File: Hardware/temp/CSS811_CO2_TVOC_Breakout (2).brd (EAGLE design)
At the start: 17.8 x 17.8 mm, 20 parts, among them U2 CCS811

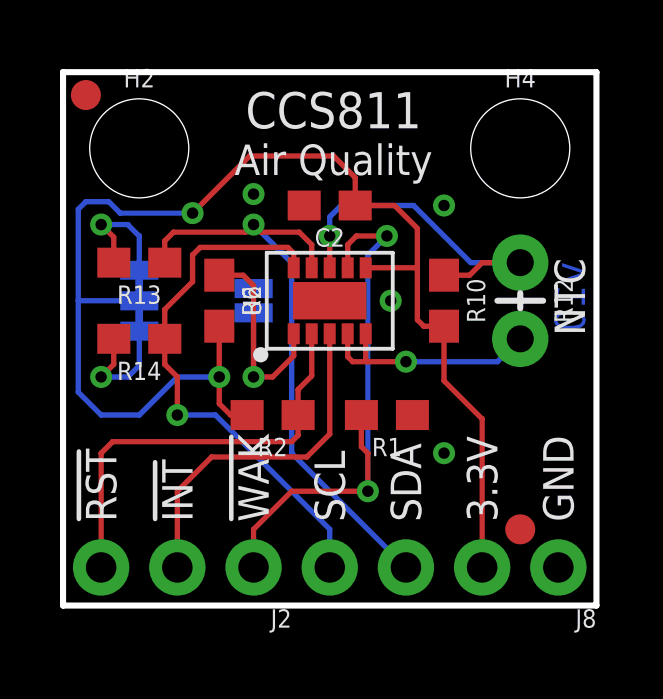
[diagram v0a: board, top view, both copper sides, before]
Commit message: Added temp library of new parts, added proper gitignore/gitattributes, switched sparkfun logo in for sparkx logo, cleaned up schematic, changed version number to v10
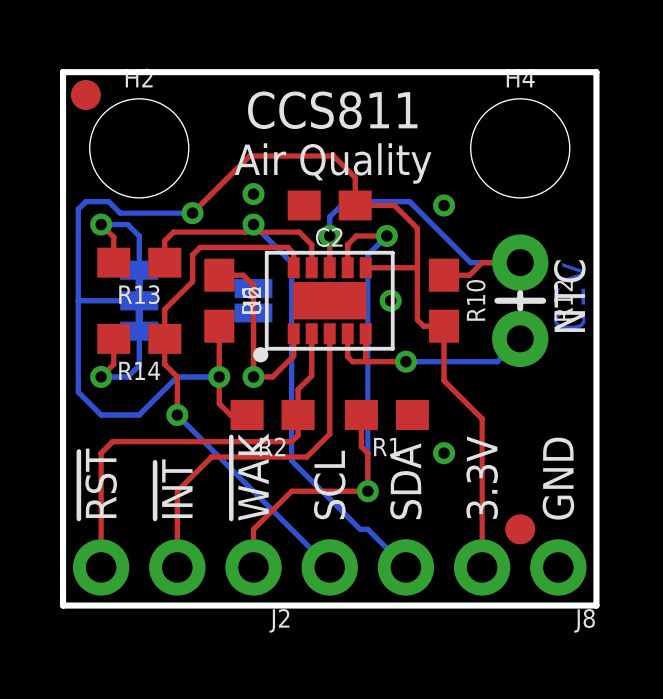
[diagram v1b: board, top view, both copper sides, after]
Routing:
- net SCL: track 17.9 -> 17.1 mm
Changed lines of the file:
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@@
 <layer number="21" name="tPlace" color="16" fill="1" visible="no" active="yes"/>
 <layer number="22" name="bPlace" color="14" fill="1" visible="yes" active="yes"/>
-<layer number="23" name="tOrigins" color="15" fill="1" visible="no" active="yes"/>
+<layer number="23" name="tOrigins" color="15" fill="1" visible="yes" active="yes"/>
 <layer number="24" name="bOrigins" color="15" fill="1" visible="yes" active="yes"/>
 <layer number="25" name="tNames" color="7" fill="1" visible="no" active="yes"/>
@@
 <wire x1="3.81" y1="7.62" x2="3.81" y2="6.35" width="0.1778" layer="1"/>
 <via x="3.81" y="6.35" extent="1-16" drill="0.381"/>
-<wire x1="3.81" y1="6.35" x2="5.08" y2="6.35" width="0.1778" layer="16"/>
-<wire x1="5.08" y1="6.35" x2="8.89" y2="2.54" width="0.1778" layer="16"/>
-<wire x1="8.89" y1="2.54" x2="8.89" y2="1.27" width="0.1778" layer="16"/>
+<wire x1="3.81" y1="6.35" x2="8.89" y2="1.27" width="0.1778" layer="16"/>
 <contactref element="U2" pad="10"/>
 <wire x1="7.69" y1="11.26" x2="7.69" y2="11.741" width="0.1778" layer="1"/>
@@
 <wire x1="3.683" y1="12.446" x2="3.39" y2="12.153" width="0.1778" layer="1"/>
 <wire x1="3.39" y1="11.43" x2="3.39" y2="12.153" width="0.1778" layer="1"/>
-<wire x1="11.43" y1="1.27" x2="7.62" y2="5.08" width="0.1778" layer="16"/>
+<wire x1="11.43" y1="1.27" x2="10.16" y2="2.54" width="0.1778" layer="16"/>
+<wire x1="10.16" y1="2.54" x2="9.906" y2="2.54" width="0.1778" layer="16"/>
+<wire x1="9.906" y1="2.54" x2="7.62" y2="4.826" width="0.1778" layer="16"/>
 <via x="6.35" y="12.7" extent="1-16" drill="0.381"/>
 <contactref element="U2" pad="9"/>
@@
 <wire x1="3.683" y1="12.446" x2="6.096" y2="12.446" width="0.1778" layer="1"/>
 <wire x1="6.096" y1="12.446" x2="6.35" y2="12.7" width="0.1778" layer="1"/>
-<wire x1="7.62" y1="5.08" x2="7.62" y2="11.43" width="0.1778" layer="16"/>
+<wire x1="7.62" y1="4.826" x2="7.62" y2="11.43" width="0.1778" layer="16"/>
 <wire x1="7.62" y1="11.43" x2="6.35" y2="12.7" width="0.1778" layer="16"/>
 </signal>
@@
 <contactref element="U2" pad="8"/>
 <wire x1="8.89" y1="11.26" x2="8.89" y2="12.319" width="0.1778" layer="1"/>
-<wire x1="9.271" y1="13.335" x2="8.89" y2="12.954" width="0.1778" layer="16"/>
+<wire x1="9.398" y1="13.462" x2="8.89" y2="12.954" width="0.1778" layer="16"/>
 <wire x1="8.89" y1="12.954" x2="8.89" y2="12.319" width="0.1778" layer="16"/>
 <wire x1="15.24" y1="11.43" x2="13.589" y2="11.43" width="0.1778" layer="16"/>
-<wire x1="13.589" y1="11.43" x2="11.684" y2="13.335" width="0.1778" layer="16"/>
-<wire x1="11.684" y1="13.335" x2="9.271" y2="13.335" width="0.1778" layer="16"/>
+<wire x1="13.589" y1="11.43" x2="11.557" y2="13.462" width="0.1778" layer="16"/>
+<wire x1="11.557" y1="13.462" x2="9.398" y2="13.462" width="0.1778" layer="16"/>
 </signal>
 <signal name="!INT">
